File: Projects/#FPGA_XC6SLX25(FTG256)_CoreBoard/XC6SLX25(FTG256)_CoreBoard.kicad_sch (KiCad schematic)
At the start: 1 part, among them U1 XC6SLX25-FTG256

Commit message: Update XC6SLX25(FTG256)_CoreBoard
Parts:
- added J1: MTA18ASF2G72HZ-2G3A1, lib:SO-DIMM-DDR4-pcb, symbol SO-DIMM-DDR4-pcb:MTA18ASF2G72HZ-2G3A1
- U1: footprint (none) -> Package_BGA:Xilinx_FTG256
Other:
- moved on the sheet: U1A, U1B, U1C, U1D

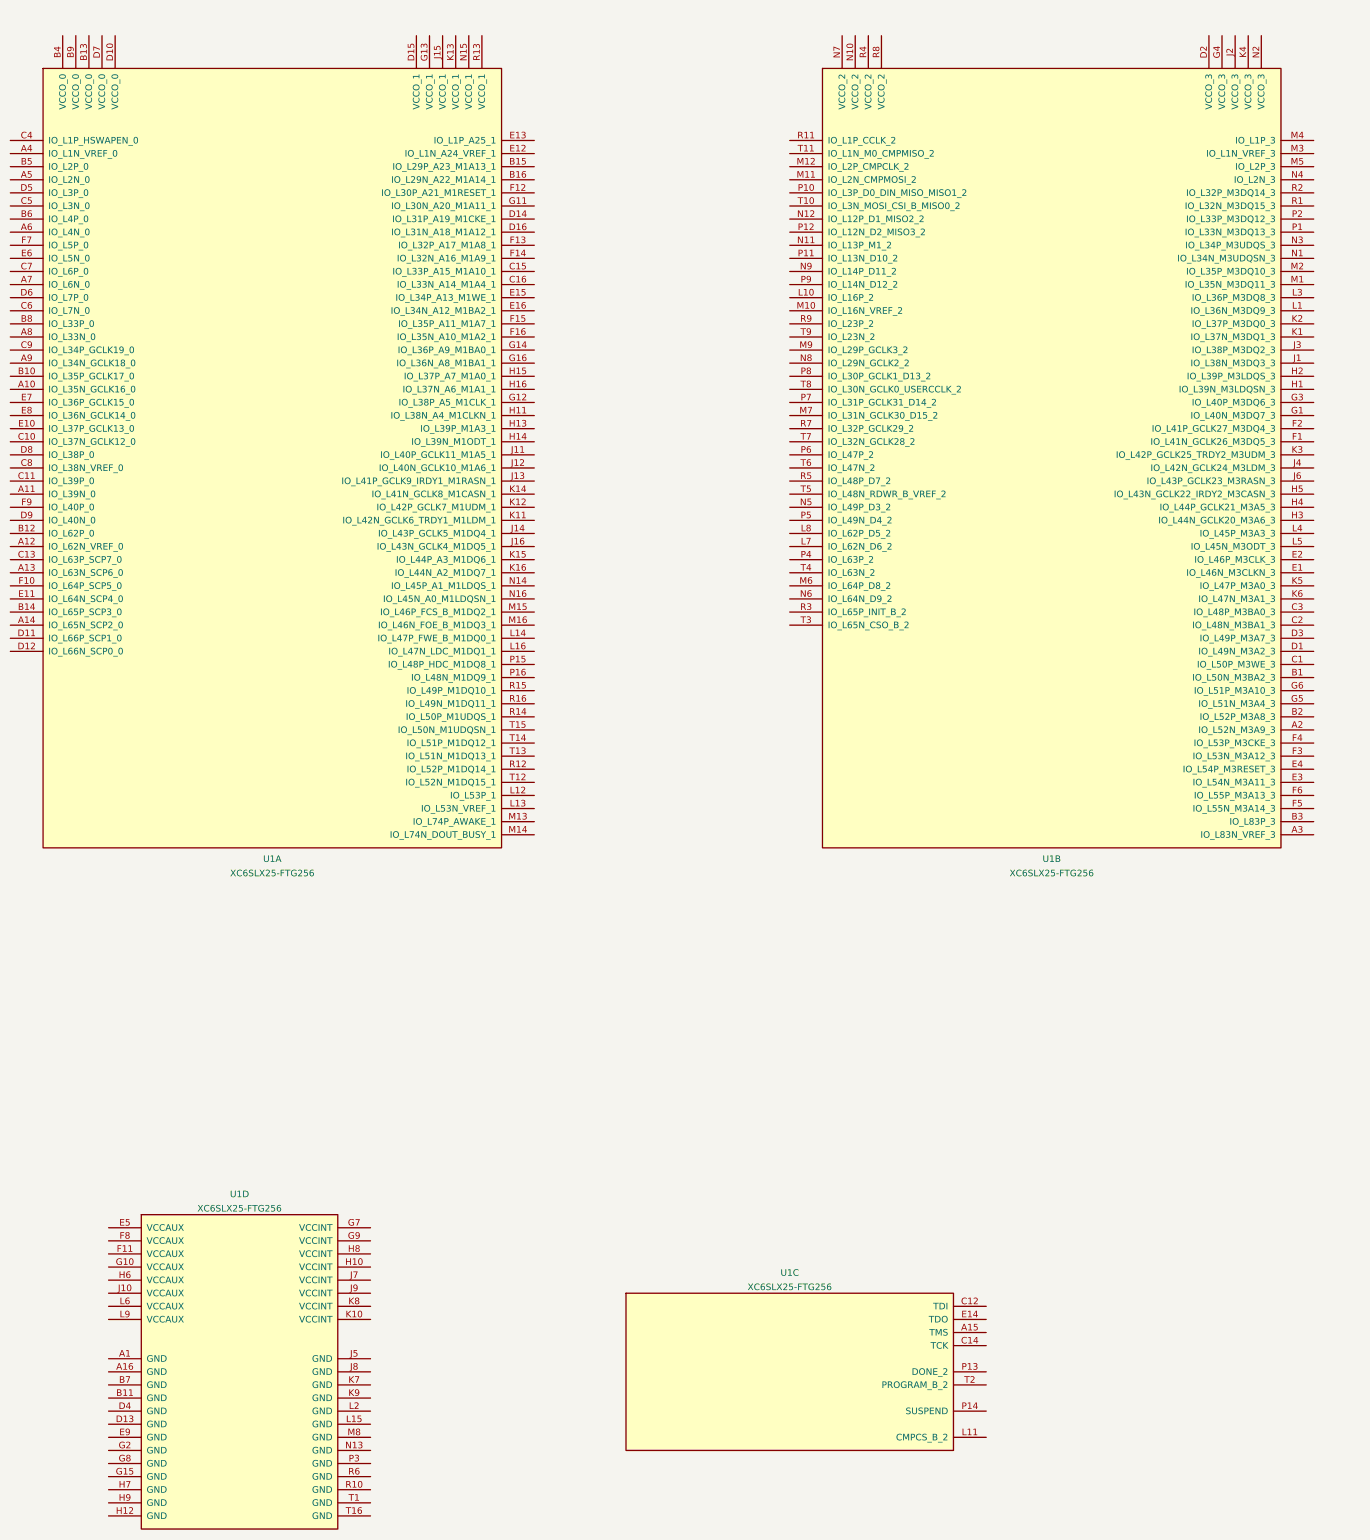
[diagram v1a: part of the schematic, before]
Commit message: Update XC6SLX25(FTG256)_CoreBoard
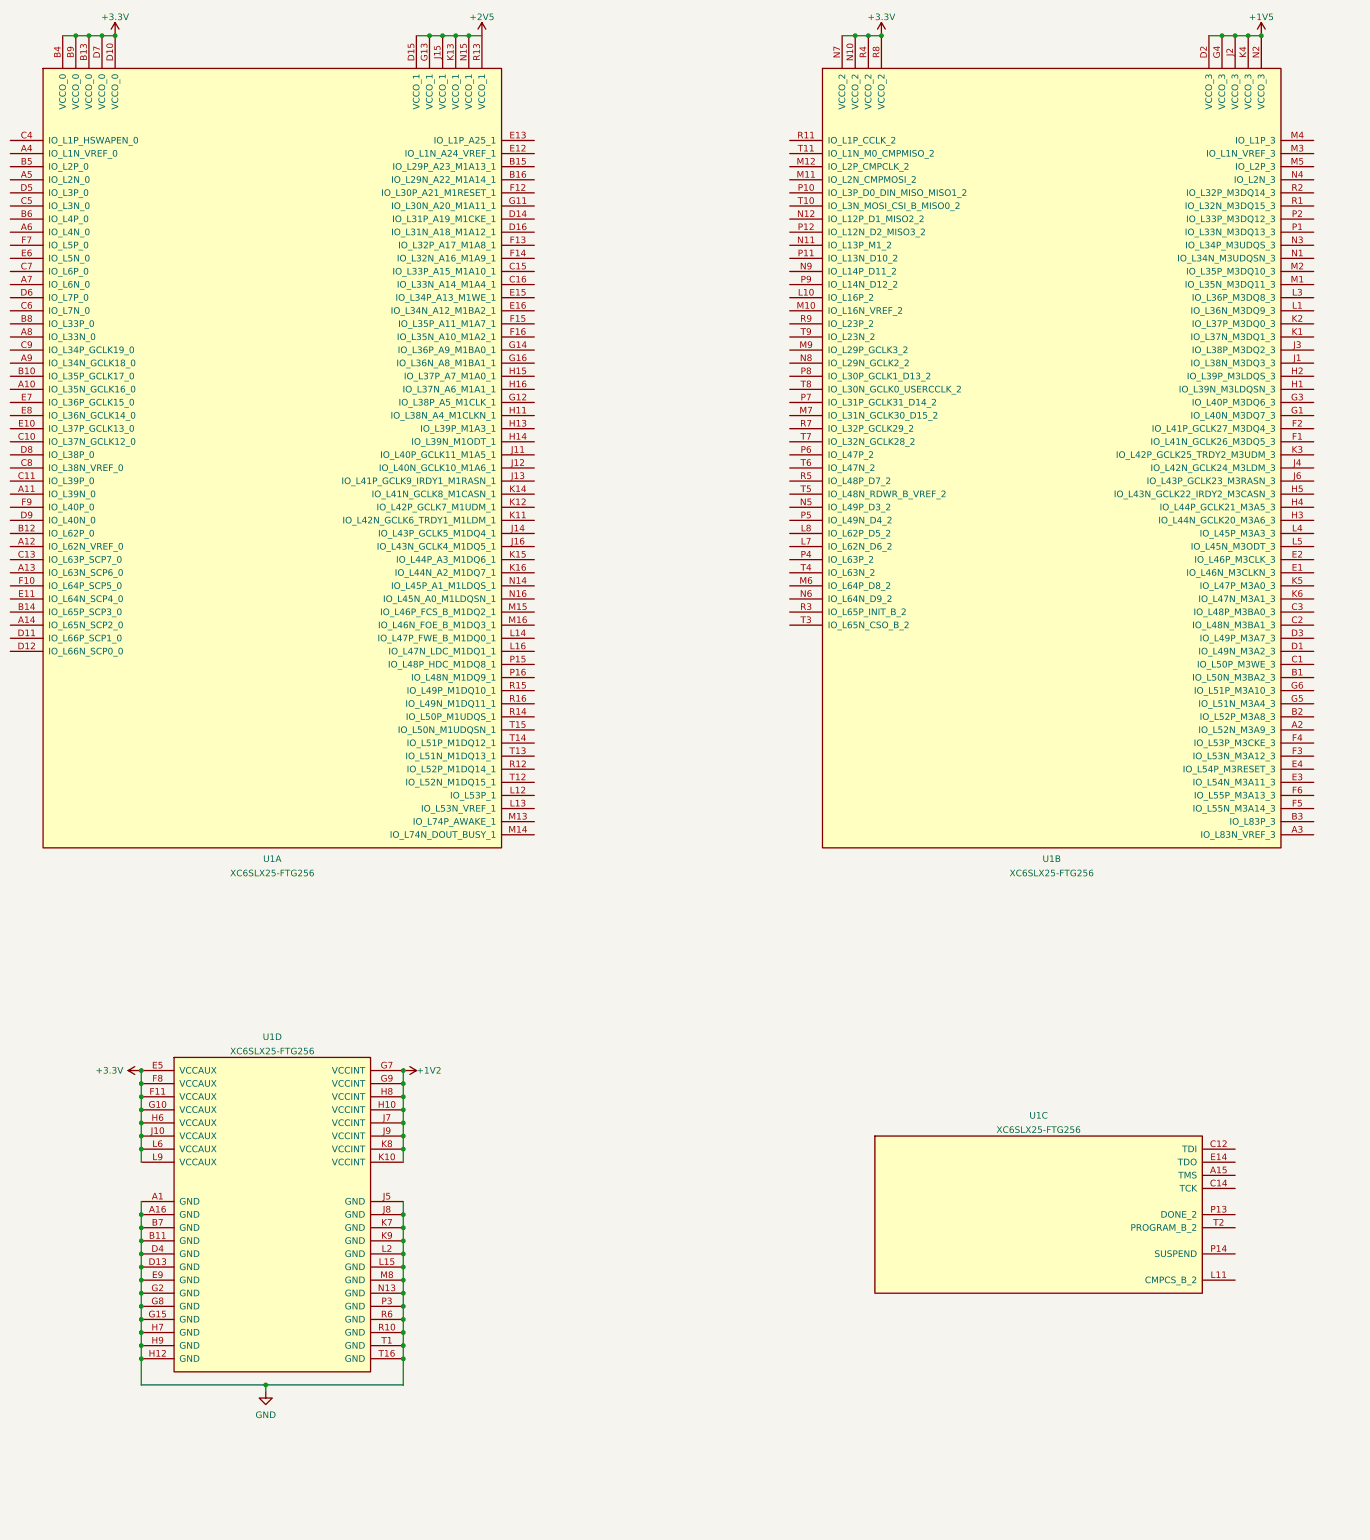
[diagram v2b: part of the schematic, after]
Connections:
- net +1V5: now reaches U1.D2 (VCCO_3)
- net +1V5: now also U1.G4 (VCCO_3), U1.J2 (VCCO_3), U1.K4 (VCCO_3), U1.N2 (VCCO_3)
- net +3V3: now reaches U1.N10 (VCCO_2)
- net +3V3: now also U1.B13 (VCCO_0), U1.B4 (VCCO_0), U1.B9 (VCCO_0), U1.D10 (VCCO_0), U1.D7 (VCCO_0), U1.E5 (VCCAUX), U1.F11 (VCCAUX), U1.F8 (VCCAUX), U1.G10 (VCCAUX), U1.H6 (VCCAUX), U1.J10 (VCCAUX), U1.L6 (VCCAUX), U1.L9 (VCCAUX), U1.N7 (VCCO_2), U1.R4 (VCCO_2), U1.R8 (VCCO_2)
- net +2V5: now reaches U1.D15 (VCCO_1)
- net +2V5: now also U1.G13 (VCCO_1), U1.J15 (VCCO_1), U1.K13 (VCCO_1), U1.N15 (VCCO_1), U1.R13 (VCCO_1)
- net GND: now reaches U1.A1 (GND)
- net GND: now also U1.A16 (GND), U1.B11 (GND), U1.B7 (GND), U1.D13 (GND), U1.D4 (GND), U1.E9 (GND), U1.G15 (GND), U1.G2 (GND), U1.G8 (GND), U1.H12 (GND), U1.H7 (GND), U1.H9 (GND), U1.J5 (GND), U1.J8 (GND), U1.K7 (GND), U1.K9 (GND), U1.L15 (GND), U1.L2 (GND), U1.M8 (GND), U1.N13 (GND), U1.P3 (GND), U1.R10 (GND), U1.R6 (GND), U1.T1 (GND), U1.T16 (GND)
- net +1V2: now reaches U1.G7 (VCCINT)
- net +1V2: now also U1.G9 (VCCINT), U1.H10 (VCCINT), U1.H8 (VCCINT), U1.J7 (VCCINT), U1.J9 (VCCINT), U1.K10 (VCCINT), U1.K8 (VCCINT)
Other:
- moved on the sheet: U1C, U1D

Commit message: Update XC6SLX25(FTG256)_CoreBoard
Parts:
- added C1, C11, C12, C14, C17, C22, C28, C3, C30, C32, C34, C36, C4, C44, C46, C47, C48, C49, C50, C51, C52, C53, C54, C55, C56, C57, C60, C67, C7, C74, C8, C81: 0.1uF, Capacitor_SMD:C_0402_1005Metric, symbol Device:C
- added C10, C13, C15, C2, C20, C24, C29, C31, C33, C35, C37, C5, C6, C9: 10nF, Capacitor_SMD:C_0402_1005Metric, symbol Device:C
- added C16, C19, C23: 0.1uF, Capacitor_SMD:C_0201_0603Metric, symbol Device:C
- added C18, C21, C25: 10nF, Capacitor_SMD:C_0201_0603Metric, symbol Device:C
- added C38, C39, C40, C41, C43, C58, C59, C65, C66, C72, C73, C79, C80: 10uF, Capacitor_SMD:C_0402_1005Metric, symbol Device:C
- added C42: 1nF, Capacitor_SMD:C_0402_1005Metric, symbol Device:C
- added C45: 4.7uF, Capacitor_SMD:C_0402_1005Metric, symbol Device:C
- added C61, C68, C75, C82: 1uF, Capacitor_SMD:C_0402_1005Metric, symbol Device:C
- added C63, C64, C70, C71, C77, C78, C84, C85: 22uF, Capacitor_SMD:C_0603_1608Metric, symbol Device:C
- added D1, D2, D3, D4: LED, LED_SMD:LED_0402_1005Metric, symbol Device:LED
- added DDR3-1: MT41J128M16JT-125, lib:DDR3-BGA96, symbol DDR3:DDR3-SDRAM-96FBGA
- added L1, L2, L3, L4: 0.47uH, Inductor_SMD:L_Taiyo-Yuden_NR-30xx, symbol Device:L
- added R1, R4: 22R, Resistor_SMD:R_0402_1005Metric, symbol Device:R
- added R10, R11, R13, R14: 100R, Resistor_SMD:R_0402_1005Metric, symbol Device:R
- added R12, R15, R16: 4K7, Resistor_SMD:R_0402_1005Metric, symbol Device:R
- added R17: 240R, Resistor_SMD:R_0402_1005Metric, symbol Device:R
- added R18, R19, R2, R21, R3, R5, R6, R7, R9: 10K, Resistor_SMD:R_0402_1005Metric, symbol Device:R
- added R20, R23, R27, R31, R35: 100K, Resistor_SMD:R_0402_1005Metric, symbol Device:R
- added R22: 5K, Resistor_SMD:R_0402_1005Metric, symbol Device:R
- added R24, R28, R32, R33, R36: 200K, Resistor_SMD:R_0402_1005Metric, symbol Device:R
- added R25: 44.2K, Resistor_SMD:R_0402_1005Metric, symbol Device:R
- added R26, R30, R34: 2K, Resistor_SMD:R_0402_1005Metric, symbol Device:R
- added R29: 63.2K, Resistor_SMD:R_0402_1005Metric, symbol Device:R
- added R37: 133.3K, Resistor_SMD:R_0402_1005Metric, symbol Device:R
- added R8: 0R, Resistor_SMD:R_0402_1005Metric, symbol Device:R
- added U2: W25Q128JVS, Package_SO:SOIC-8_5.23x5.23mm_P1.27mm, symbol Memory_Flash:W25Q128JVS
- added U3: TPS51200DRC, Package_SON:VSON-10-1EP_3x3mm_P0.5mm_EP1.65x2.4mm, symbol TPS51200DRC:TPS51200DRC
- added U4, U5, U6, U7: MP214x, lib:MP2145, symbol MP2145:MP214x
- added X1: ECS-2520MV-xxx-xx, Oscillator:Oscillator_SMD_ECS_2520MV-xxx-xx-4Pin_2.5x2.0mm, symbol Oscillator:ECS-2520MV-xxx-xx
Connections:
- net +1V2: now also C16.1, C18.1, C19.1, C21.1, C23.1, C25.1, C77.1, C78.1, L3.2, R32.1, U6.2 (OUT)
- net +1V5: now also C32.1, C33.1, C34.1, C35.1, C36.1, C37.1, C41.1, C43.1, C46.1, C47.1, C48.1, C49.1, C50.1, C51.1, C52.1, C53.1, C54.1, C55.1, C56.1, C57.1, C84.1, C85.1, DDR3-1.A1 (VDDQ), DDR3-1.A8 (VDDQ), DDR3-1.B2 (VDD), DDR3-1.C1 (VDDQ), DDR3-1.C9 (VDDQ), DDR3-1.D2 (VDDQ), DDR3-1.D9 (VDD), DDR3-1.E9 (VDDQ), DDR3-1.F1 (VDDQ), DDR3-1.G7 (VDD), DDR3-1.H2 (VDDQ), DDR3-1.H9 (VDDQ), DDR3-1.K2 (VDD), DDR3-1.K8 (VDD), DDR3-1.N1 (VDD), DDR3-1.N9 (VDD), DDR3-1.R1 (VDD), DDR3-1.R9 (VDD), L4.2, R18.1, R36.1, U3.2 (VLDOIN), U7.2 (OUT)
- net +2V5: now also C14.1, C15.1, C17.1, C20.1, C22.1, C24.1, C70.1, C71.1, L2.2, R28.1, U5.2 (OUT)
- net +3V3: now also C1.1, C10.1, C11.1, C12.1, C13.1, C2.1, C28.1, C29.1, C3.1, C30.1, C31.1, C4.1, C45.1, C5.1, C6.1, C63.1, C64.1, C7.1, C8.1, C9.1, L1.2, R2.2, R20.1, R21.2, R24.1, R3.2, R5.2, R6.2, R7.2, R9.2, U2.8 (VCC), U3.10 (VIN), U4.2 (OUT), X1.1 (Tri-State), X1.4 (VDD)
- net GND: now also C1.2, C10.2, C11.2, C12.2, C13.2, C14.2, C15.2, C16.2, C17.2, C18.2, C19.2, C2.2, C20.2, C21.2, C22.2, C23.2, C24.2, C25.2, C28.2, C29.2, C3.2, C30.2, C31.2, C32.2, C33.2, C34.2, C35.2, C36.2, C37.2, C38.2, C39.2, C4.2, C40.2, C41.2, C42.2, C43.2, C44.2, C45.2, C46.2, C47.2, C48.2, C49.2, C5.2, C50.2, C51.2, C52.2, C53.2, C54.2, C55.2, C56.2, C57.2, C58.2, C59.2, C6.2, C60.2, C61.2, C63.2, C64.2, C65.2, C66.2, C67.2, C68.2, C7.2, C70.2, C71.2, C72.2, C73.2, C74.2, C75.2, C77.2, C78.2, C79.2, C8.2, C80.2, C81.2, C82.2, C84.2, C85.2, C9.2, D1.1 (K), D2.1 (K), D3.1 (K), D4.1 (K), DDR3-1.A9 (VSS), DDR3-1.B1 (VSSQ), DDR3-1.B3 (VSS), DDR3-1.B9 (VSSQ), DDR3-1.D1 (VSSQ), DDR3-1.D8 (VSSQ), DDR3-1.E1 (VSS), DDR3-1.E2 (VSSQ), DDR3-1.E8 (VSSQ), DDR3-1.F9 (VSSQ), DDR3-1.G1 (VSSQ), DDR3-1.G8 (VSS), DDR3-1.G9 (VSSQ), DDR3-1.J2 (VSS), DDR3-1.J8 (VSS), DDR3-1.M1 (VSS), DDR3-1.M9 (VSS), DDR3-1.P1 (VSS), DDR3-1.P9 (VSS), DDR3-1.T1 (VSS), DDR3-1.T9 (VSS), R1.2, R12.2, R13.2, R15.2, R16.2, R17.2, R19.2, R25.2, R29.2, R33.2, R37.2, R4.2, R8.2, U2.4 (GND), U3.11 (GND), U3.4 (GND), U3.8 (GND), U4.10 (GND), U4.11 (GND), U4.12 (GND), U5.10 (GND), U5.11 (GND), U5.12 (GND), U6.10 (GND), U6.11 (GND), U6.12 (GND), U7.10 (GND), U7.11 (GND), U7.12 (GND), X1.2 (GND)
- net DDR_A9: now reaches U1.A2 (IO_L52N_M3A9_3)
- net DDR_A9: now also DDR3-1.R3 (A9)
- net DDR_VREF: now reaches U1.A3 (IO_L83N_VREF_3)
- net DDR_VREF: now also U1.M3 (IO_L1N_VREF_3), C44.1, DDR3-1.H1 (VREFDQ), DDR3-1.M8 (VREFCA), U3.6 (REFOUT)
- net DDR_BA2: now reaches U1.B1 (IO_L50N_M3BA2_3)
- net DDR_BA2: now also DDR3-1.M3 (BA2)
- net DDR_A8: now reaches U1.B2 (IO_L52P_M3A8_3)
- net DDR_A8: now also DDR3-1.T8 (A8)
- net DDR_CS1: now reaches U1.B3 (IO_L83P_3)
- net DDR_CS1: now also DDR3-1.L2 (~{CS}), R13.1
- net DDR_WE: now reaches U1.C1 (IO_L50P_M3WE_3)
- net DDR_WE: now also DDR3-1.L3 (~{WE})
- net DDR_BA1: now reaches U1.C2 (IO_L48N_M3BA1_3)
- net DDR_BA1: now also DDR3-1.N8 (BA1)
- net DDR_BA0: now reaches U1.C3 (IO_L48P_M3BA0_3)
- net DDR_BA0: now also DDR3-1.M2 (BA0)
- net DDR_A2: now reaches U1.D1 (IO_L49N_M3A2_3)
- net DDR_A2: now also DDR3-1.P3 (A2)
- net DDR_A7: now reaches U1.D3 (IO_L49P_M3A7_3)
- net DDR_A7: now also DDR3-1.R2 (A7)
- net DDR_CLK-: now reaches U1.E1 (IO_L46N_M3CLKN_3)
- net DDR_CLK-: now also DDR3-1.K7 (~{CK}), R14.2
- net DDR_CLK+: now reaches U1.E2 (IO_L46P_M3CLK_3)
- net DDR_CLK+: now also DDR3-1.J7 (CK), R14.1
- net DDR_A11: now reaches U1.E3 (IO_L54N_M3A11_3)
- net DDR_A11: now also DDR3-1.R7 (A11)
- net DDR_RESET: now reaches U1.E4 (IO_L54P_M3RESET_3)
- net DDR_RESET: now also DDR3-1.T2 (~{RESET}), R12.1
- net DDR_D5: now reaches U1.F1 (IO_L41N_GCLK26_M3DQ5_3)
- net DDR_D5: now also DDR3-1.H8 (DQ5)
- net DDR_D4: now reaches U1.F2 (IO_L41P_GCLK27_M3DQ4_3)
- net DDR_D4: now also DDR3-1.H3 (DQ4)
- net DDR_A12: now reaches U1.F3 (IO_L53N_M3A12_3)
- net DDR_A12: now also DDR3-1.N7 (A12/~{BC})
- net DDR_CKE: now reaches U1.F4 (IO_L53P_M3CKE_3)
- net DDR_CKE: now also DDR3-1.K9 (CKE), R15.1
- net DDR_A14: now reaches U1.F5 (IO_L55N_M3A14_3)
- net DDR_A14: now also DDR3-1.T7 (A14)
- net DDR_A13: now reaches U1.F6 (IO_L55P_M3A13_3)
- net DDR_A13: now also DDR3-1.T3 (A13)
- net DDR_D7: now reaches U1.G1 (IO_L40N_M3DQ7_3)
- net DDR_D7: now also DDR3-1.H7 (DQ7)
- net DDR_D6: now reaches U1.G3 (IO_L40P_M3DQ6_3)
- net DDR_D6: now also DDR3-1.G2 (DQ6)
- net DDR_A4: now reaches U1.G5 (IO_L51N_M3A4_3)
- net DDR_A4: now also DDR3-1.P8 (A4)
- net DDR_A10: now reaches U1.G6 (IO_L51P_M3A10_3)
- net DDR_A10: now also DDR3-1.L7 (A10/AP)
- net DDR_LDQS-: now reaches U1.H1 (IO_L39N_M3LDQSN_3)
- net DDR_LDQS-: now also DDR3-1.G3 (~{LDQS}), R10.2
- net DDR_LDQS+: now reaches U1.H2 (IO_L39P_M3LDQS_3)
- net DDR_LDQS+: now also DDR3-1.F3 (LDQS), R10.1
- net DDR_A6: now reaches U1.H3 (IO_L44N_GCLK20_M3A6_3)
- net DDR_A6: now also DDR3-1.R8 (A6)
- net DDR_A5: now reaches U1.H4 (IO_L44P_GCLK21_M3A5_3)
- net DDR_A5: now also DDR3-1.P2 (A5)
- net DDR_~{CAS}: now reaches U1.H5 (IO_L43N_GCLK22_IRDY2_M3CASN_3)
- net DDR_~{CAS}: now also DDR3-1.K3 (~{CAS})
- net DDR_D3: now reaches U1.J1 (IO_L38N_M3DQ3_3)
- net DDR_D3: now also DDR3-1.F8 (DQ3)
- net DDR_D2: now reaches U1.J3 (IO_L38P_M3DQ2_3)
- net DDR_D2: now also DDR3-1.F2 (DQ2)
- net DDR_LDM: now reaches U1.J4 (IO_L42N_GCLK24_M3LDM_3)
- net DDR_LDM: now also DDR3-1.E7 (LDM)
- net DDR_~{RAS}: now reaches U1.J6 (IO_L43P_GCLK23_M3RASN_3)
- net DDR_~{RAS}: now also DDR3-1.J3 (~{RAS})
- net DDR_D1: now reaches U1.K1 (IO_L37N_M3DQ1_3)
- net DDR_D1: now also DDR3-1.F7 (DQ1)
- net DDR_D0: now reaches U1.K2 (IO_L37P_M3DQ0_3)
- net DDR_D0: now also DDR3-1.E3 (DQ0)
- net DDR_UDM: now reaches U1.K3 (IO_L42P_GCLK25_TRDY2_M3UDM_3)
- net DDR_UDM: now also DDR3-1.D3 (UDM)
- net DDR_A0: now reaches U1.K5 (IO_L47P_M3A0_3)
- net DDR_A0: now also DDR3-1.N3 (A0)
- net DDR_A1: now reaches U1.K6 (IO_L47N_M3A1_3)
- net DDR_A1: now also DDR3-1.P7 (A1)
- net DDR_D9: now reaches U1.L1 (IO_L36N_M3DQ9_3)
- net DDR_D9: now also DDR3-1.C3 (DQ9)
- net DDR_D8: now reaches U1.L3 (IO_L36P_M3DQ8_3)
- net DDR_D8: now also DDR3-1.D7 (DQ8)
- net DDR_A3: now reaches U1.L4 (IO_L45P_M3A3_3)
- net DDR_A3: now also DDR3-1.N2 (A3)
- net DDR_ODT: now reaches U1.L5 (IO_L45N_M3ODT_3)
- net DDR_ODT: now also DDR3-1.K1 (ODT), R16.1
- net DDR_D11: now reaches U1.M1 (IO_L35N_M3DQ11_3)
- net DDR_D11: now also DDR3-1.C2 (DQ11)
- net DDR_D10: now reaches U1.M2 (IO_L35P_M3DQ10_3)
- net DDR_D10: now also DDR3-1.C8 (DQ10)
- net DDR_UDQS-: now reaches U1.N1 (IO_L34N_M3UDQSN_3)
- net DDR_UDQS-: now also DDR3-1.B7 (~{UDQS}), R11.2
- net at U1.N11 (IO_L13P_M1_2): now also R4.1
- net Flash_MISO_2: now reaches U1.N12 (IO_L12P_D1_MISO2_2)
- net Flash_MISO_2: now also U2.3 (IO2)
- net DDR_UDQS+: now reaches U1.N3 (IO_L34P_M3UDQS_3)
- net DDR_UDQS+: now also DDR3-1.C7 (UDQS), R11.1
- net DDR_D13: now reaches U1.P1 (IO_L33N_M3DQ13_3)
- net DDR_D13: now also DDR3-1.A2 (DQ13)
- net Flash_MISO_1: now reaches U1.P10 (IO_L3P_D0_DIN_MISO_MISO1_2)
- net Flash_MISO_1: now also U2.2 (DO(IO1))
- net Flash_MISO_3: now reaches U1.P12 (IO_L12N_D2_MISO3_2)
- net Flash_MISO_3: now also U2.7 (IO3)
- net DDR_D12: now reaches U1.P2 (IO_L33P_M3DQ12_3)
- net DDR_D12: now also DDR3-1.A7 (DQ12)
- net GCLK: now reaches U1.P7 (IO_L31P_GCLK31_D14_2)
- net GCLK: now also X1.3 (OUT)
- net DDR_D15: now reaches U1.R1 (IO_L32N_M3DQ15_3)
- net DDR_D15: now also DDR3-1.A3 (DQ15)
- net Flash_CLK: now reaches U1.R11 (IO_L1P_CCLK_2)
- net Flash_CLK: now also U2.6 (CLK)
- net DDR_D14: now reaches U1.R2 (IO_L32P_M3DQ14_3)
- net DDR_D14: now also DDR3-1.B8 (DQ14)
- net at U1.R3 (IO_L65P_INIT_B_2): now also R5.1
- net Flash_MOSI: now reaches U1.T10 (IO_L3N_MOSI_CSI_B_MISO0_2)
- net Flash_MOSI: now also U2.5 (DI(IO0))
- net at U1.T11 (IO_L1N_M0_CMPMISO_2): now also R3.1
- net Flash_CS: now reaches U1.T3 (IO_L65N_CSO_B_2)
- net Flash_CS: now also R2.1, U2.1 (~{CS})
- net TCK: now reaches J1.1
- net TCK: now also U1.C14 (TCK)
- net TMS: now reaches J1.3
- net TMS: now also U1.A15 (TMS)
- net TDO: now reaches J1.5
- net TDO: now also U1.E14 (TDO)
- net TDI: now reaches J1.7
- net TDI: now also U1.C12 (TDI)
- net at U1.C4 (IO_L1P_HSWAPEN_0): now also R1.1
- net at U1.L11 (CMPCS_B_2): now also R9.1
- net at U1.P13 (DONE_2): now also R6.1
- net at U1.P14 (SUSPEND): now also R8.1
- net at U1.T2 (PROGRAM_B_2): now also R7.1
- new net: L4.1, U7.1 (SW), U7.9 (SW)
- new net: R36.2, R37.1, U7.3 (FB)
- new net: R35.2, U7.5 (EN)
- new net: C82.1, U7.6 (MODE)
- new net: D4.2 (A), R34.2, U7.7 (PG)
- new net: R20.2, U3.9 (PGOOD)
- new net: L3.1, U6.1 (SW), U6.9 (SW)
- new net: R32.2, R33.1, U6.3 (FB)
- new net: R31.2, U6.5 (EN)
- new net: C75.1, U6.6 (MODE)
- new net: D3.2 (A), R30.2, U6.7 (PG)
- new net: DDR3-1.L8 (ZQ), R17.1
- new net: L1.1, U4.1 (SW), U4.9 (SW)
- new net: C42.1, R18.2, R19.1, U3.1 (REFIN)
- new net: R21.1, U3.7 (EN)
- new net: R28.2, R29.1, U5.3 (FB)
- new net: D1.2 (A), R22.2, U4.7 (PG)
- new net: L2.1, U5.1 (SW), U5.9 (SW)
- new net: R24.2, R25.1, U4.3 (FB)
- new net: C61.1, U4.6 (MODE)
- new net: R23.2, U4.5 (EN)
- new net: R27.2, U5.5 (EN)
- new net: C68.1, U5.6 (MODE)
- new net: D2.2 (A), R26.2, U5.7 (PG)
- new net 5V: C58.1, C59.1, C60.1, C65.1, C66.1, C67.1, C72.1, C73.1, C74.1, C79.1, C80.1, C81.1, R22.1, R23.1, R26.1, R27.1, R30.1, R31.1, R34.1, R35.1, U4.8 (VIN), U5.8 (VIN), U6.8 (VIN), U7.8 (VIN)
- new net DDR_VTT: C38.1, C39.1, C40.1, U3.3 (VO), U3.5 (VOSNS)
- no-connect marks 0 -> 8
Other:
- note added: "10uF Cap-Load for prevent auto-exciting"
- note added: "DDR3 2Gb(128M*16) x1"
- note added: "DIMM DDR4 Connector"
- moved on the sheet: J1A, J1B, J1C, J1D, U1A, U1B, U1C, U1D

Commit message: Update XC6SLX25(FTG256)_CoreBoard
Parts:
- added R38, R39: R, Resistor_SMD:R_0402_1005Metric, symbol Device:R
- added RN1, RN10, RN2, RN3, RN4, RN5, RN6, RN7, RN8, RN9: R_Pack04, Resistor_SMD:R_Array_Concave_4x0402, symbol Device:R_Pack04
- added RN11, RN12: R_Pack02, Resistor_SMD:R_Array_Convex_2x0402, symbol Device:R_Pack02
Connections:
- net DDR_A0: now also RN1.8 (R1.2)
- net DDR_A1: now also RN1.7 (R2.2)
- net DDR_A10: now also RN3.6 (R3.2)
- net DDR_A11: now also RN3.5 (R4.2)
- net DDR_A12: now also RN4.7 (R2.2)
- net DDR_A13: now also RN4.6 (R3.2)
- net DDR_A14: now also RN4.5 (R4.2)
- net DDR_A2: now also RN1.6 (R3.2)
- net DDR_A3: now also RN1.5 (R4.2)
- net DDR_A4: now also RN2.8 (R1.2)
- net DDR_A5: now also RN2.7 (R2.2)
- net DDR_A6: now also RN2.6 (R3.2)
- net DDR_A7: now also RN2.5 (R4.2)
- net DDR_A8: now also RN3.8 (R1.2)
- net DDR_A9: now also RN3.7 (R2.2)
- net DDR_BA0: now also RN5.5 (R4.2)
- net DDR_BA1: now also RN4.8 (R1.2)
- net DDR_BA2: now also RN5.6 (R3.2)
- net DDR_CKE: now also RN6.8 (R1.2)
- net DDR_CS1: now also RN5.7 (R2.2)
- net DDR_D0: now also RN7.8 (R1.2); no longer U1.K2 (IO_L37P_M3DQ0_3)
- net DDR_D1: now also RN7.5 (R4.2); no longer U1.K1 (IO_L37N_M3DQ1_3)
- net DDR_D10: now also RN9.6 (R3.2); no longer U1.M2 (IO_L35P_M3DQ10_3)
- net DDR_D11: now also RN9.8 (R1.2); no longer U1.M1 (IO_L35N_M3DQ11_3)
- net DDR_D12: now also RN10.7 (R2.2); no longer U1.P2 (IO_L33P_M3DQ12_3)
- net DDR_D13: now also RN10.5 (R4.2); no longer U1.P1 (IO_L33N_M3DQ13_3)
- net DDR_D14: now also RN10.8 (R1.2); no longer U1.R2 (IO_L32P_M3DQ14_3)
- net DDR_D15: now also RN10.6 (R3.2); no longer U1.R1 (IO_L32N_M3DQ15_3)
- net DDR_D2: now also RN7.7 (R2.2); no longer U1.J3 (IO_L38P_M3DQ2_3)
- net DDR_D3: now also RN7.6 (R3.2); no longer U1.J1 (IO_L38N_M3DQ3_3)
- net DDR_D4: now also RN8.8 (R1.2); no longer U1.F2 (IO_L41P_GCLK27_M3DQ4_3)
- net DDR_D5: now also RN8.7 (R2.2); no longer U1.F1 (IO_L41N_GCLK26_M3DQ5_3)
- net DDR_D6: now also RN8.6 (R3.2); no longer U1.G3 (IO_L40P_M3DQ6_3)
- net DDR_D7: now also RN8.5 (R4.2); no longer U1.G1 (IO_L40N_M3DQ7_3)
- net DDR_D8: now also RN9.5 (R4.2); no longer U1.L3 (IO_L36P_M3DQ8_3)
- net DDR_D9: now also RN9.7 (R2.2); no longer U1.L1 (IO_L36N_M3DQ9_3)
- net DDR_LDM: now also R39.1; no longer U1.J4 (IO_L42N_GCLK24_M3LDM_3)
- net DDR_LDQS+: now also RN12.3 (R2.2); no longer U1.H2 (IO_L39P_M3LDQS_3)
- net DDR_LDQS-: now also RN12.4 (R1.2); no longer U1.H1 (IO_L39N_M3LDQSN_3)
- net DDR_ODT: now also RN5.8 (R1.2)
- net DDR_UDM: now also R38.1; no longer U1.K3 (IO_L42P_GCLK25_TRDY2_M3UDM_3)
- net DDR_UDQS+: now also RN11.4 (R1.2); no longer U1.N3 (IO_L34P_M3UDQS_3)
- net DDR_UDQS-: now also RN11.3 (R2.2); no longer U1.N1 (IO_L34N_M3UDQSN_3)
- net DDR_VTT: now also RN1.1 (R1.1), RN1.2 (R2.1), RN1.3 (R3.1), RN1.4 (R4.1), RN2.1 (R1.1), RN2.2 (R2.1), RN2.3 (R3.1), RN2.4 (R4.1), RN3.1 (R1.1), RN3.2 (R2.1), RN3.3 (R3.1), RN3.4 (R4.1), RN4.1 (R1.1), RN4.2 (R2.1), RN4.3 (R3.1), RN4.4 (R4.1), RN5.1 (R1.1), RN5.2 (R2.1), RN5.3 (R3.1), RN5.4 (R4.1), RN6.1 (R1.1), RN6.2 (R2.1), RN6.3 (R3.1), RN6.4 (R4.1)
- net DDR_WE: now also RN6.7 (R2.2)
- net DDR_~{CAS}: now also RN6.6 (R3.2)
- net DDR_~{RAS}: now also RN6.5 (R4.2)
- new net DDR_MD0: RN7.1 (R1.1), U1.K2 (IO_L37P_M3DQ0_3)
- new net DDR_MD1: RN7.2 (R2.1), U1.K1 (IO_L37N_M3DQ1_3)
- new net DDR_MD10: RN9.1 (R1.1), U1.M2 (IO_L35P_M3DQ10_3)
- new net DDR_MD11: RN9.2 (R2.1), U1.M1 (IO_L35N_M3DQ11_3)
- new net DDR_MD12: RN10.3 (R3.1), U1.P2 (IO_L33P_M3DQ12_3)
- new net DDR_MD13: RN10.4 (R4.1), U1.P1 (IO_L33N_M3DQ13_3)
- new net DDR_MD14: RN10.1 (R1.1), U1.R2 (IO_L32P_M3DQ14_3)
- new net DDR_MD15: RN10.2 (R2.1), U1.R1 (IO_L32N_M3DQ15_3)
- new net DDR_MD2: RN7.3 (R3.1), U1.J3 (IO_L38P_M3DQ2_3)
- new net DDR_MD3: RN7.4 (R4.1), U1.J1 (IO_L38N_M3DQ3_3)
- new net DDR_MD4: RN8.4 (R4.1), U1.F2 (IO_L41P_GCLK27_M3DQ4_3)
- new net DDR_MD5: RN8.3 (R3.1), U1.F1 (IO_L41N_GCLK26_M3DQ5_3)
- new net DDR_MD6: RN8.2 (R2.1), U1.G3 (IO_L40P_M3DQ6_3)
- new net DDR_MD7: RN8.1 (R1.1), U1.G1 (IO_L40N_M3DQ7_3)
- new net DDR_MD8: RN9.4 (R4.1), U1.L3 (IO_L36P_M3DQ8_3)
- new net DDR_MD9: RN9.3 (R3.1), U1.L1 (IO_L36N_M3DQ9_3)
- new net DDR_MLDM: R39.2, U1.J4 (IO_L42N_GCLK24_M3LDM_3)
- new net DDR_MLDQS+: RN12.2 (R2.1), U1.H2 (IO_L39P_M3LDQS_3)
- new net DDR_MLDQS-: RN12.1 (R1.1), U1.H1 (IO_L39N_M3LDQSN_3)
- new net DDR_MUDM: R38.2, U1.K3 (IO_L42P_GCLK25_TRDY2_M3UDM_3)
- new net DDR_MUDQS+: RN11.1 (R1.1), U1.N3 (IO_L34P_M3UDQS_3)
- new net DDR_MUDQS-: RN11.2 (R2.1), U1.N1 (IO_L34N_M3UDQSN_3)
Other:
- note added: "Preivate swap DQ0 and DQ8"
- moved on the sheet: C38, C39, C40, C41, C42, C43, C44, C45, C46, C47, C48, C49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
